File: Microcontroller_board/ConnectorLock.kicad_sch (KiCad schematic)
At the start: 11 parts, among them J3 Conn_01x04_Pin, Q3 BC817, U3 4N35

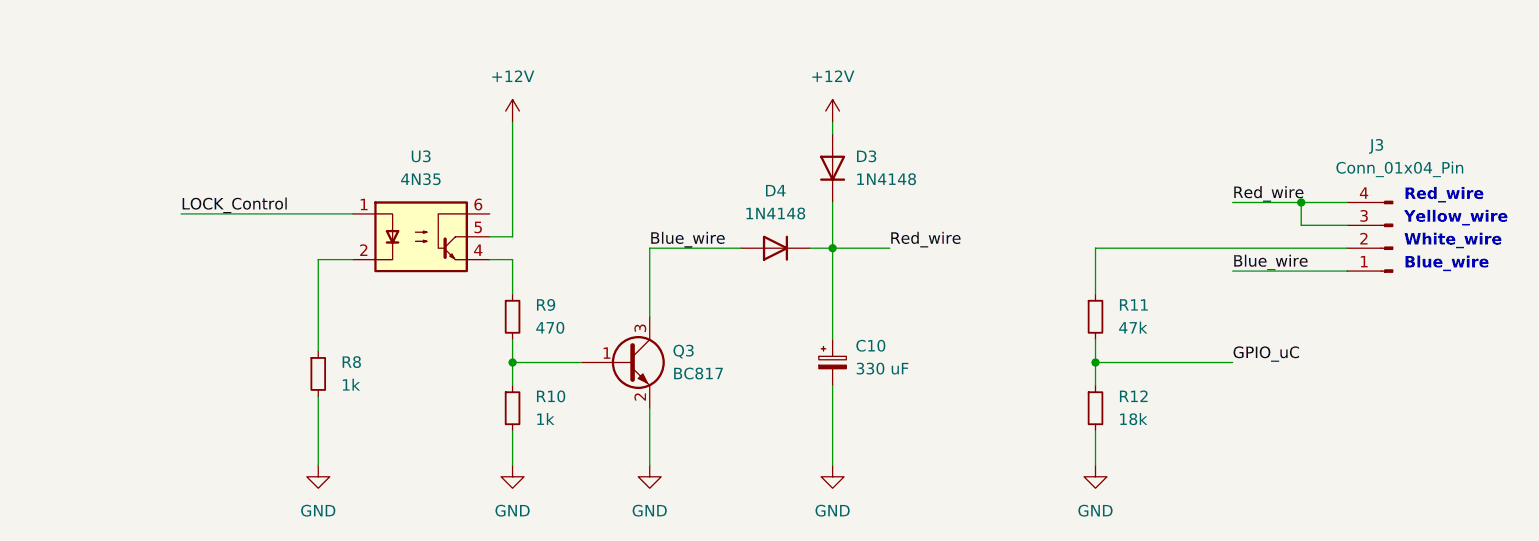
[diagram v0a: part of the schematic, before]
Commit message: Added more pages, CP and RS485
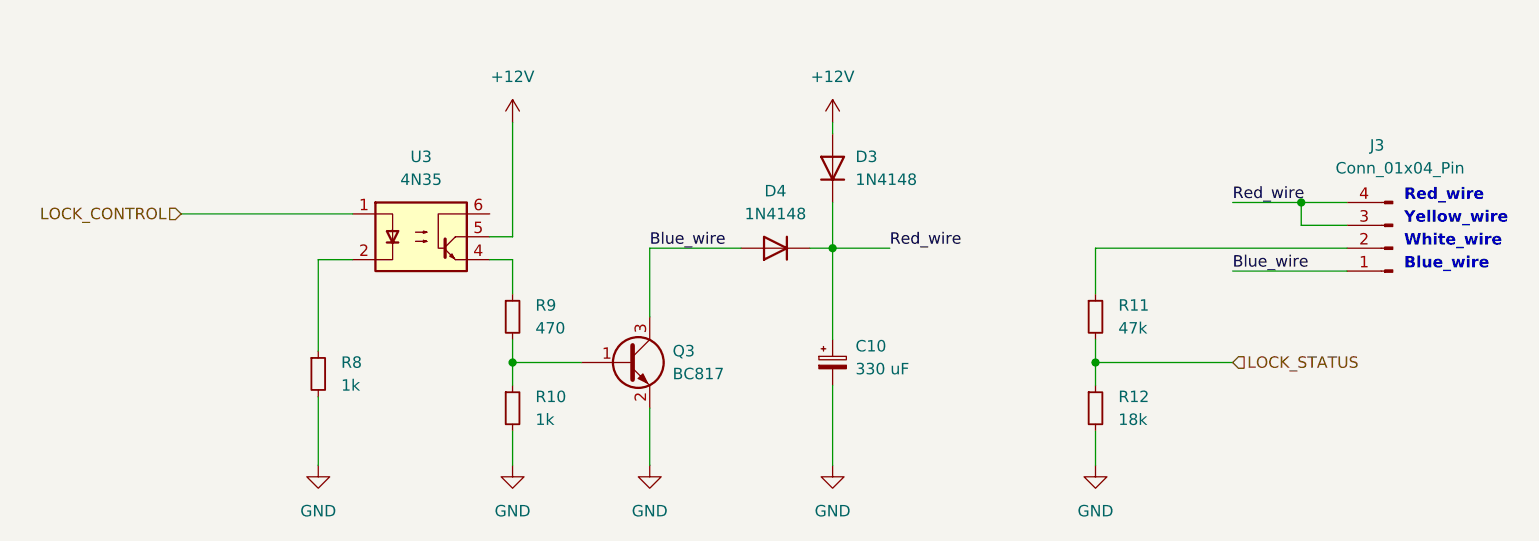
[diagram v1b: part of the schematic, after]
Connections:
- net GPIO_uC renamed LOCK_STATUS
- net LOCK_Control renamed LOCK_CONTROL
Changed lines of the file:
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@@
-    (effects (font (size 1.27 1.27)) (justify left bottom))
-  )
-  (label "GPIO_uC" (at 198.12 104.14 0) (fields_autoplaced)
     (effects (font (size 1.27 1.27)) (justify left bottom))
   )
@@
     (effects (font (size 1.27 1.27)) (justify left bottom))
   )
-  (label "LOCK_Control" (at 81.28 87.63 0) (fields_autoplaced)
-    (effects (font (size 1.27 1.27)) (justify left bottom))
+  (hierarchical_label "LOCK_CONTROL" (shape input) (at 81.28 87.63 180) (fields_autoplaced)
+    (effects (font (size 1.27 1.27)) (justify right))
+  )
+  (hierarchical_label "LOCK_STATUS" (shape input) (at 198.12 104.14 0) (fields_autoplaced)
+    (effects (font (size 1.27 1.27)) (justify left))
   )
   (symbol (lib_id "power:GND") (at 133.35 115.57 0) (unit 1)

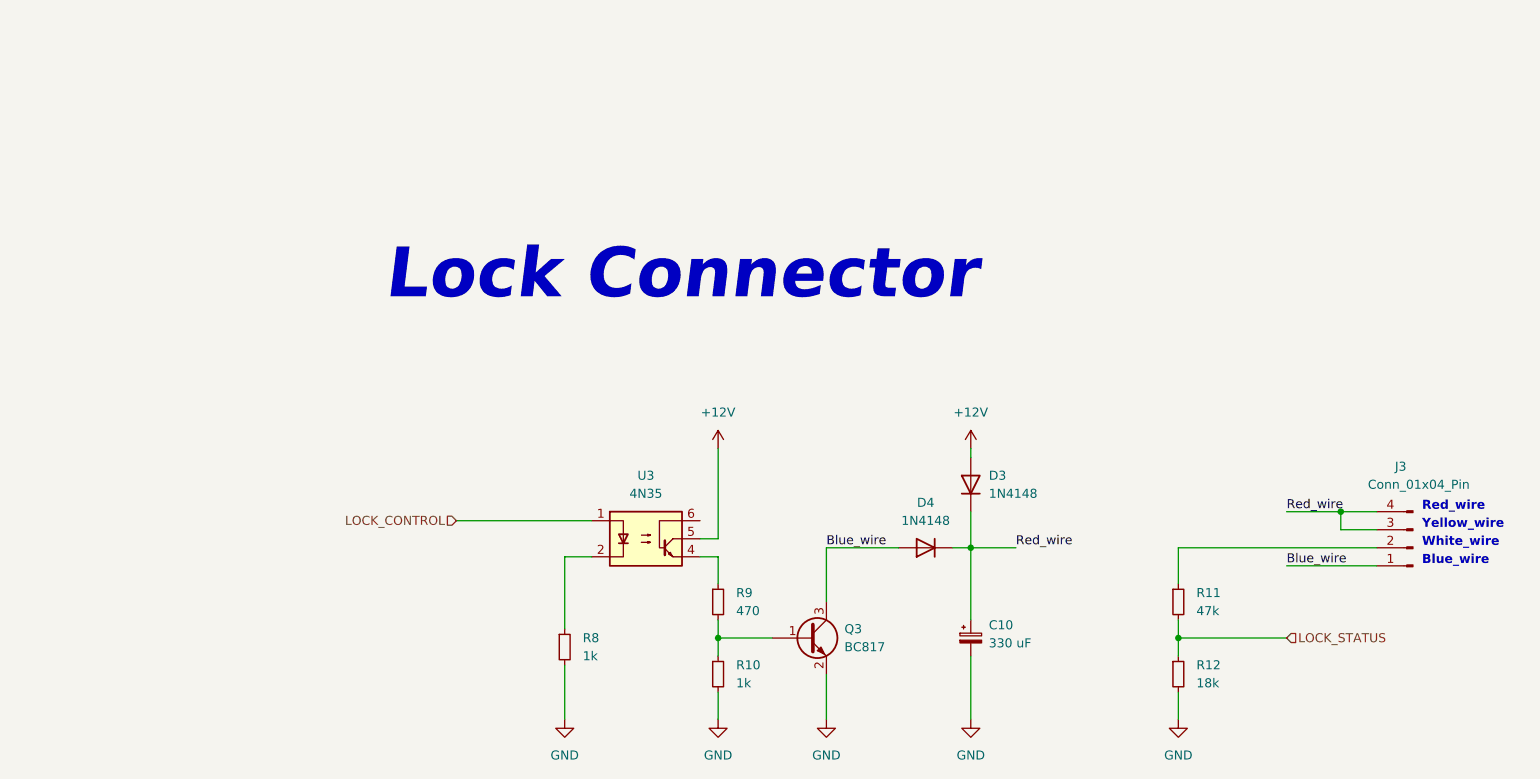
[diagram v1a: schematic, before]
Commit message: Added two more leds and make the schematic a little bit prettier
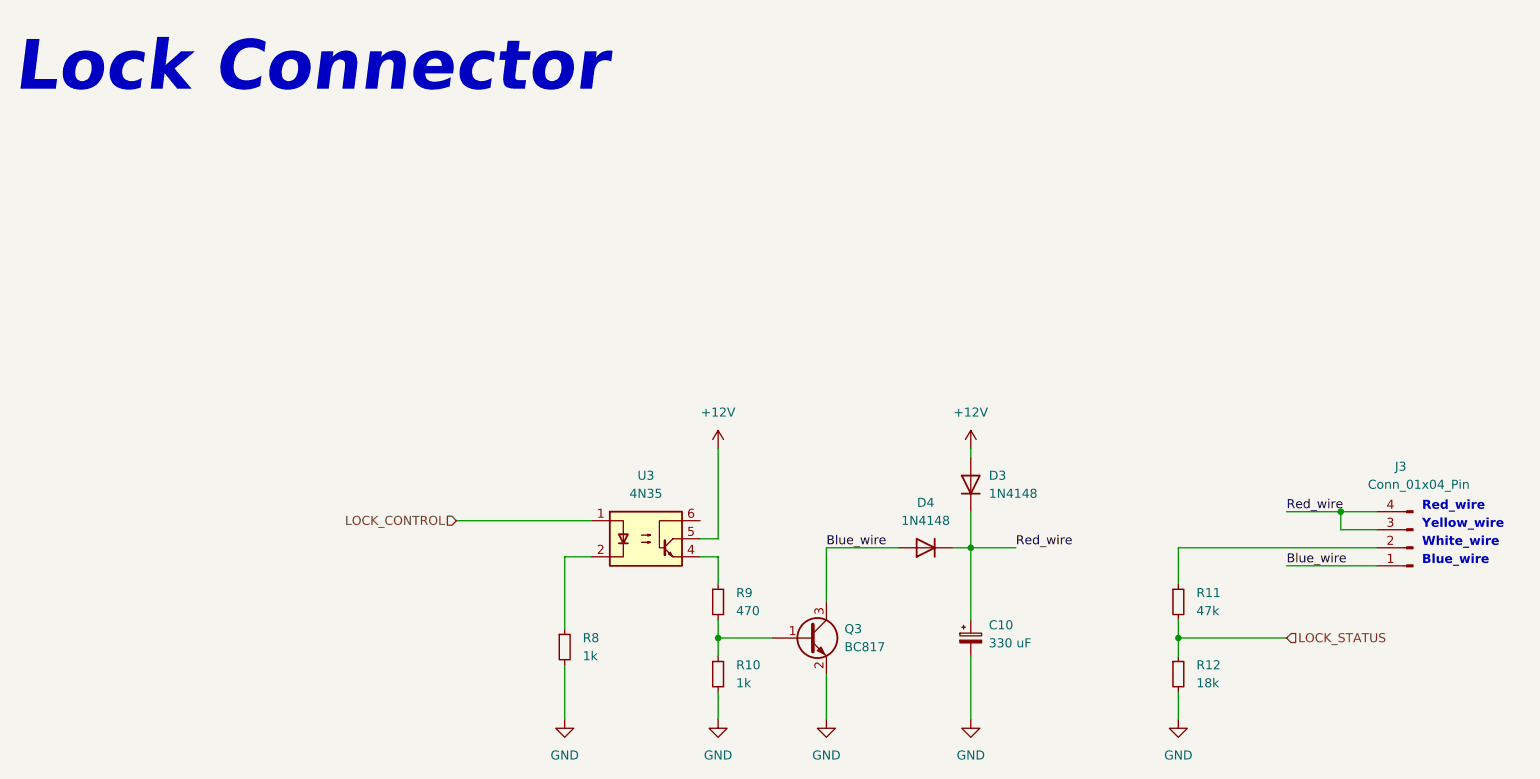
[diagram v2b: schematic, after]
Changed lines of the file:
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@@
     (effects (font (size 1.27 1.27) bold) (justify left bottom))
   )
-  (text "Lock Connector\n" (at 71.12 57.15 0)
+  (text "Lock Connector\n" (at 19.05 27.94 0)
     (effects (font (size 7 7) (thickness 1.2) bold italic) (justify left bottom))
   )
